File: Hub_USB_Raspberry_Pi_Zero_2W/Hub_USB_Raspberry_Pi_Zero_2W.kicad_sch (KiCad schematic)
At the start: 5 parts, among them U1 CH334F

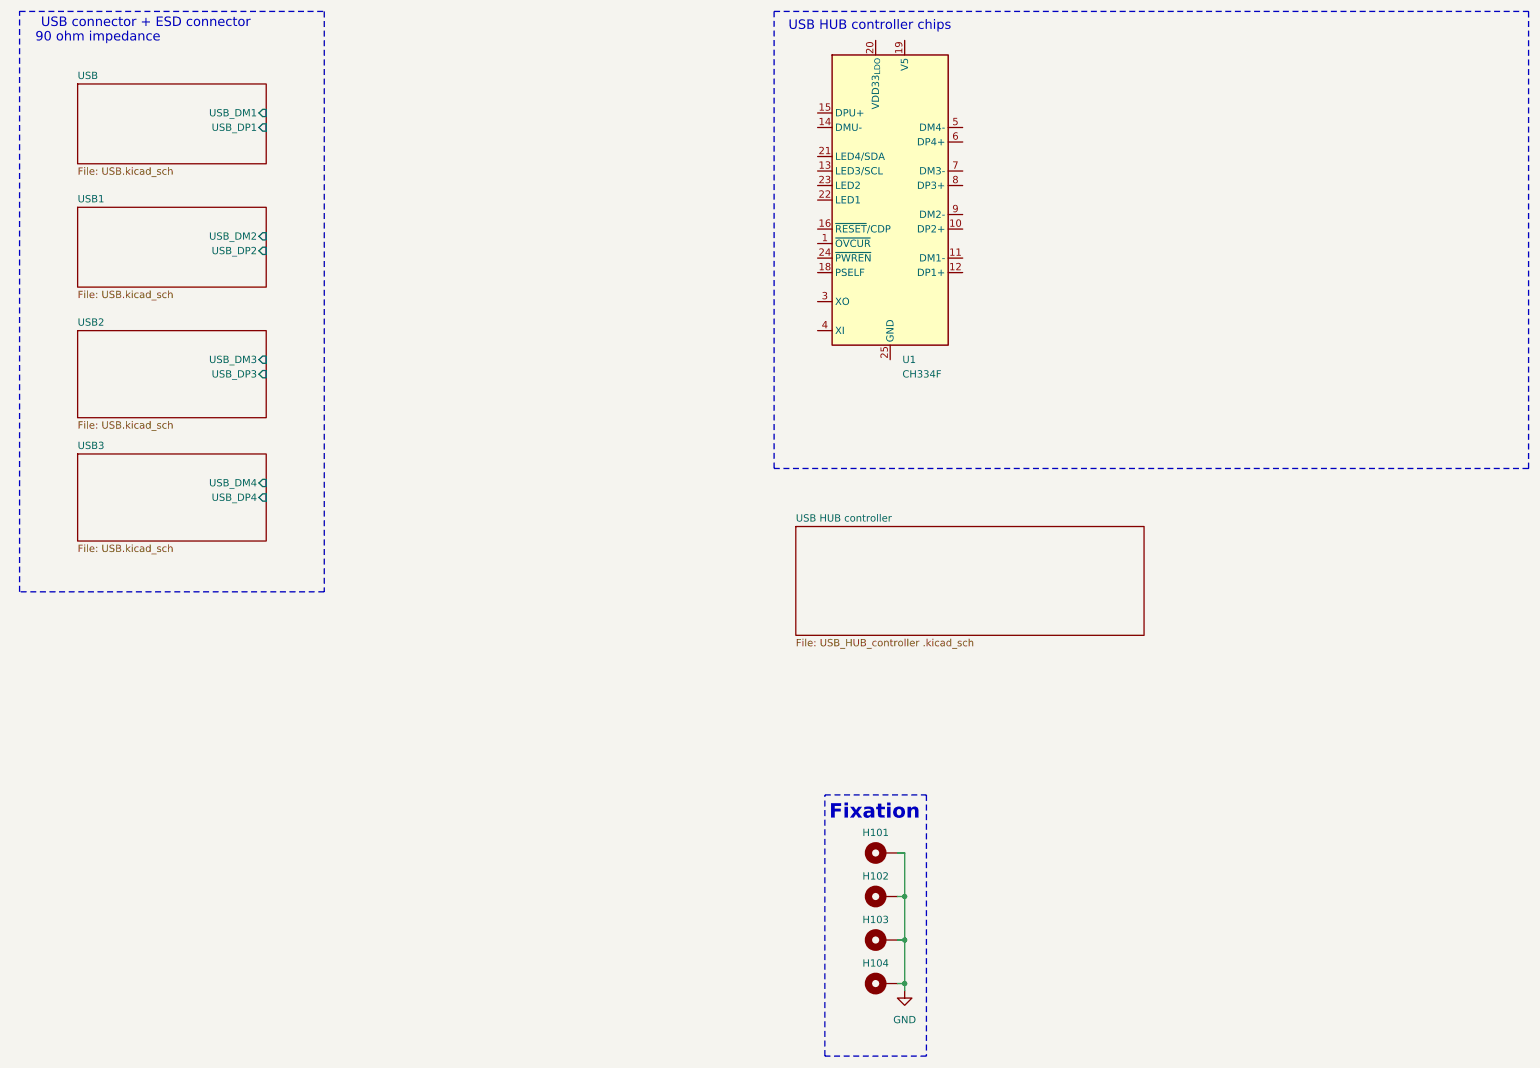
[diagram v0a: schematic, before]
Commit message: Update kicad HUB
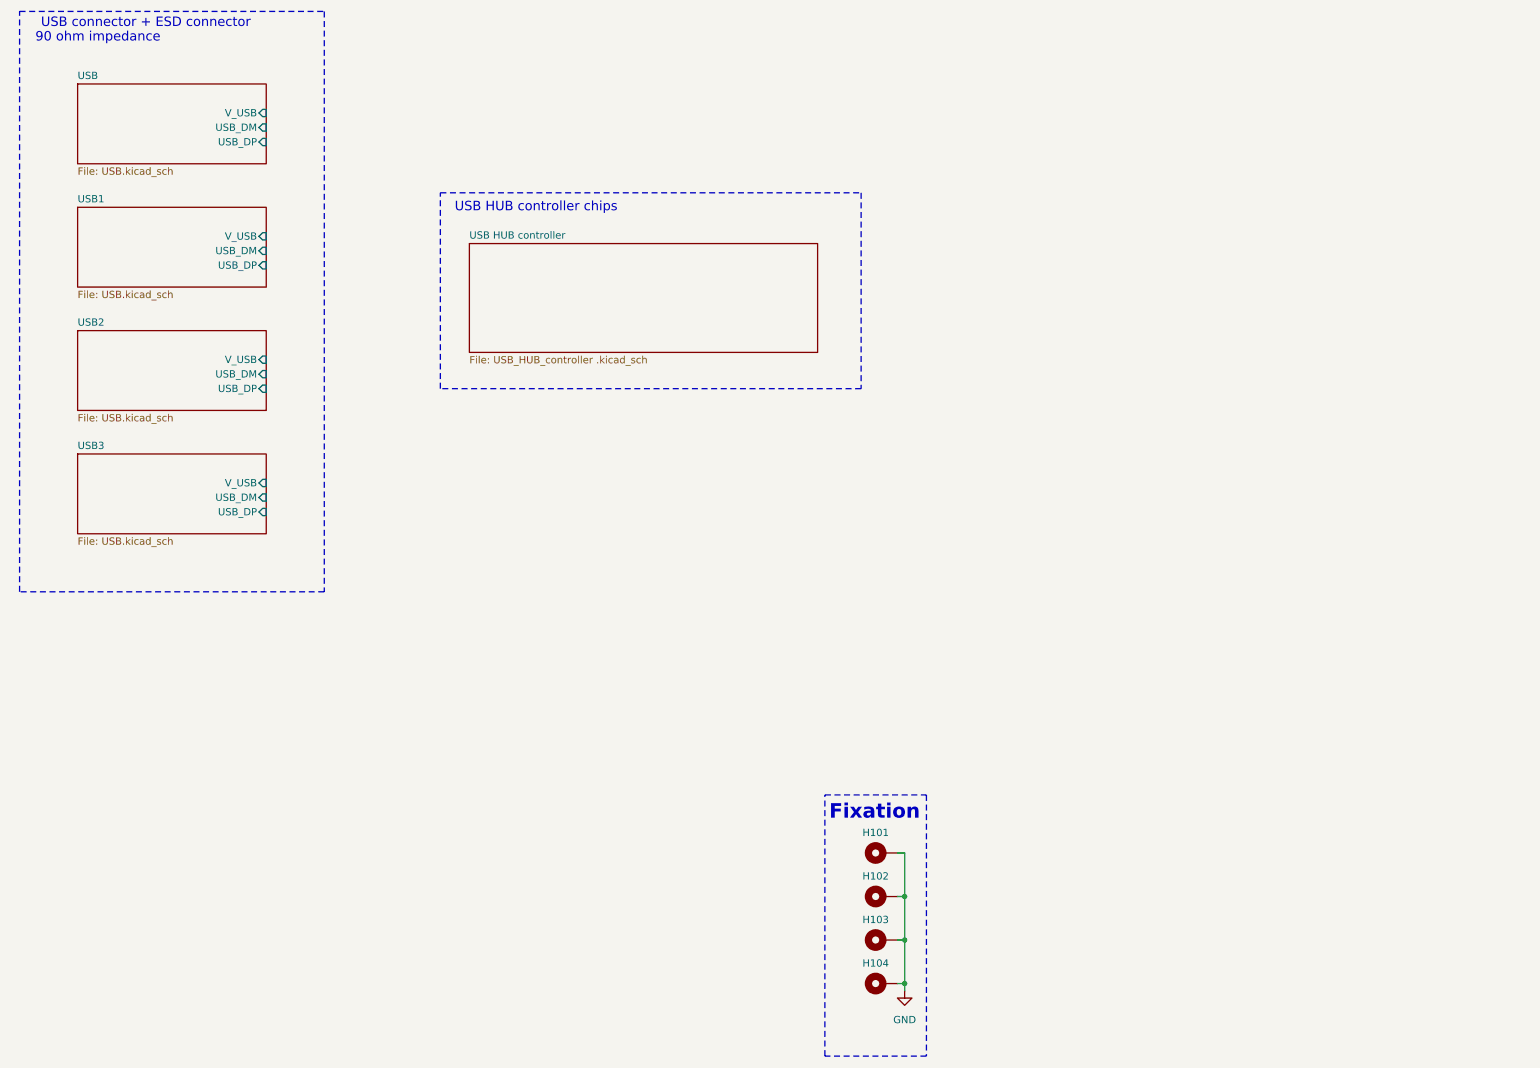
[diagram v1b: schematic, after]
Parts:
- removed U1: CH334F, Package_DFN_QFN:QFN-24-1EP_4x4mm_P0.5mm_EP2.7x2.7mm, symbol Interface_USB:CH334F
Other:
- sheet USB ports: added USB_DM, USB_DP, V_USB; removed USB_DM1, USB_DP1
- sheet USB1 ports: added USB_DM, USB_DP, V_USB; removed USB_DM2, USB_DP2
- sheet USB2 ports: added USB_DM, USB_DP, V_USB; removed USB_DM3, USB_DP3
- sheet USB3 ports: added USB_DM, USB_DP, V_USB; removed USB_DM4, USB_DP4
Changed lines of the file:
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@@
 	)
 	(rectangle
-		(start 147.32 13.97)
-		(end 279.4 93.98)
+		(start 88.9 45.72)
+		(end 162.56 80.01)
 		(stroke
 			(width 0)
@@
 	(text "USB HUB controller chips"
 		(exclude_from_sim no)
-		(at 164.084 16.51 0)
+		(at 105.664 48.26 0)
 		(effects
 			(font
@@
 		)
 	)
-	(symbol
-		(lib_id "Interface_USB:CH334F")
-		(at 167.64 46.99 0)
-		(unit 1)
-		(exclude_from_sim no)
-		(in_bom yes)
-		(on_board yes)
-		(dnp no)
-		(fields_autoplaced yes)
-		(property "Reference" "U1"
-			(at 169.7833 74.93 0)
-			(effects
-				(font
-					(size 1.27 1.27)
-				)
-				(justify left)
-			)
-		)
-		(property "Value" "CH334F"
-			(at 169.7833 77.47 0)
-			(effects
-				(font
-					(size 1.27 1.27)
-				)
-				(justify left)
-			)
-		)
-		(property "Footprint" "Package_DFN_QFN:QFN-24-1EP_4x4mm_P0.5mm_EP2.7x2.7mm"
-			(at 137.16 74.93 0)
-			(effects
-				(font
-					(size 1.27 1.27)
-				)
-				(justify left)
-				(hide yes)
-			)
-		)
-		(property "Datasheet" "https://www.wch-ic.com/downloads/file/327.html"
-			(at 167.64 13.97 0)
-			(effects
-				(font
-					(size 1.27 1.27)
-				)
-				(hide yes)
-			)
-		)
-		(property "Description" "USB HUB controller, QFN-24"
-			(at 167.64 46.99 0)
-			(effects
-				(font
-					(size 1.27 1.27)
-				)
-				(hide yes)
-			)
-		)
-		(pin "2"
-		)
-		(pin "19"
-		)
-		(pin "17"
-		)
-		(pin "22"
-		)
-		(pin "23"
-		)
-		(pin "9"
-		)
-		(pin "15"
-		)
-		(pin "4"
-		)
-		(pin "7"
-		)
-		(pin "5"
-		)
-		(pin "6"
-		)
-		(pin "10"
-		)
-		(pin "3"
-		)
-		(pin "25"
-		)
-		(pin "13"
-		)
-		(pin "21"
-		)
-		(pin "20"
-		)
-		(pin "14"
-		)
-		(pin "24"
-		)
-		(pin "8"
-		)
-		(pin "1"
-		)
-		(pin "16"
-		)
-		(pin "12"
-		)
-		(pin "11"
-		)
-		(pin "18"
-		)
-		(instances
-			(project ""
-				(path "/7e321a74-9d7c-485f-8c03-6a7893ec6c14"
-					(reference "U1")
-					(unit 1)
-				)
-			)
-		)
-	)
 	(sheet
-		(at 151.13 104.14)
+		(at 93.98 54.61)
 		(size 60.96 19.05)
 		(exclude_from_sim no)
@@
 		)
 		(property "Sheetname" "USB HUB controller"
-			(at 151.13 103.4284 0)
+			(at 93.98 53.8984 0)
 			(effects
 				(font
@@
 		)
 		(property "Sheetfile" "USB_HUB_controller .kicad_sch"
-			(at 151.13 123.7746 0)
+			(at 93.98 74.2446 0)
 			(effects
 				(font
@@
 	(sheet
 		(at 25.4 91.44)
-		(size 33.02 15.24)
+		(size 33.02 13.97)
 		(exclude_from_sim no)
 		(in_bom yes)
@@
 		)
 		(property "Sheetfile" "USB.kicad_sch"
-			(at 25.4 107.2646 0)
+			(at 25.4 105.9946 0)
 			(effects
 				(font
@@
 			)
 		)
-		(pin "USB_DM4" input
+		(pin "USB_DM" input
+			(at 58.42 99.06 0)
+			(effects
+				(font
+					(size 1.27 1.27)
+				)
+				(justify right)
+			)
+		)
+		(pin "USB_DP" input
+			(at 58.42 101.6 0)
+			(effects
+				(font
+					(size 1.27 1.27)
+				)
+				(justify right)
+			)
+		)
+		(pin "V_USB" input
 			(at 58.42 96.52 0)
-			(effects
-				(font
-					(size 1.27 1.27)
-				)
-				(justify right)
-			)
-		)
-		(pin "USB_DP4" input
-			(at 58.42 99.06 0)
 			(effects
 				(font
@@
 	(sheet
 		(at 25.4 69.85)
-		(size 33.02 15.24)
+		(size 33.02 13.97)
 		(exclude_from_sim no)
 		(in_bom yes)
@@
 		)
 		(property "Sheetfile" "USB.kicad_sch"
-			(at 25.4 85.6746 0)
+			(at 25.4 84.4046 0)
 			(effects
 				(font
@@
 			)
 		)
-		(pin "USB_DM3" input
+		(pin "USB_DM" input
+			(at 58.42 77.47 0)
+			(effects
+				(font
+					(size 1.27 1.27)
+				)
+				(justify right)
+			)
+		)
+		(pin "USB_DP" input
+			(at 58.42 80.01 0)
+			(effects
+				(font
+					(size 1.27 1.27)
+				)
+				(justify right)
+			)
+		)
+		(pin "V_USB" input
 			(at 58.42 74.93 0)
-			(effects
-				(font
-					(size 1.27 1.27)
-				)
-				(justify right)
-			)
-		)
-		(pin "USB_DP3" input
-			(at 58.42 77.47 0)
 			(effects
 				(font
@@
 			)
 		)
-		(pin "USB_DM1" input
+		(pin "USB_DM" input
+			(at 58.42 34.29 0)
+			(effects
+				(font
+					(size 1.27 1.27)
+				)
+				(justify right)
+			)
+		)
+		(pin "USB_DP" input
+			(at 58.42 36.83 0)
+			(effects
+				(font
+					(size 1.27 1.27)
+				)
+				(justify right)
+			)
+		)
+		(pin "V_USB" input
 			(at 58.42 31.75 0)
-			(effects
-				(font
-					(size 1.27 1.27)
-				)
-				(justify right)
-			)
-		)
-		(pin "USB_DP1" input
-			(at 58.42 34.29 0)
 			(effects
 				(font
@@
 			)
 		)
-		(pin "USB_DM2" input
+		(pin "USB_DM" input
+			(at 58.42 55.88 0)
+			(effects
+				(font
+					(size 1.27 1.27)
+				)
+				(justify right)
+			)
+		)
+		(pin "USB_DP" input
+			(at 58.42 58.42 0)
+			(effects
+				(font
+					(size 1.27 1.27)
+				)
+				(justify right)
+			)
+		)
+		(pin "V_USB" input
 			(at 58.42 53.34 0)
 			(effects
 				(font
-					(size 1.27 1.27)
-				)
-				(justify right)
-			)
-		)
-		(pin "USB_DP2" input
-			(at 58.42 55.88 0)
-			(effects
-				(font

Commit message: CB avançage
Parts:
- H101, H102, H103, H104: footprint MountingHole:MountingHole_3.2mm_M3_Pad_Via -> MountingHole:MountingHole_2.5mm_Pad_Via
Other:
- sheet USB HUB controller ports: added DM1-, DM2-, DM3-, DM4-, DP1+, DP2+, DP3+, DP4+, VBUS; removed none
